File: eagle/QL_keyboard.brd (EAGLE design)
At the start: 66 x 51.4 mm, 40 parts, among them J1 USB-A-S, J2 AVR_SPI_PRG_6TESTPOINTS, U2 3.3V/150mA, U3 MAX3421ESMD, U4 ATMEGA328P_TQFP, U5 TXB0108PW-TSSOP20, Y1 8MHZ

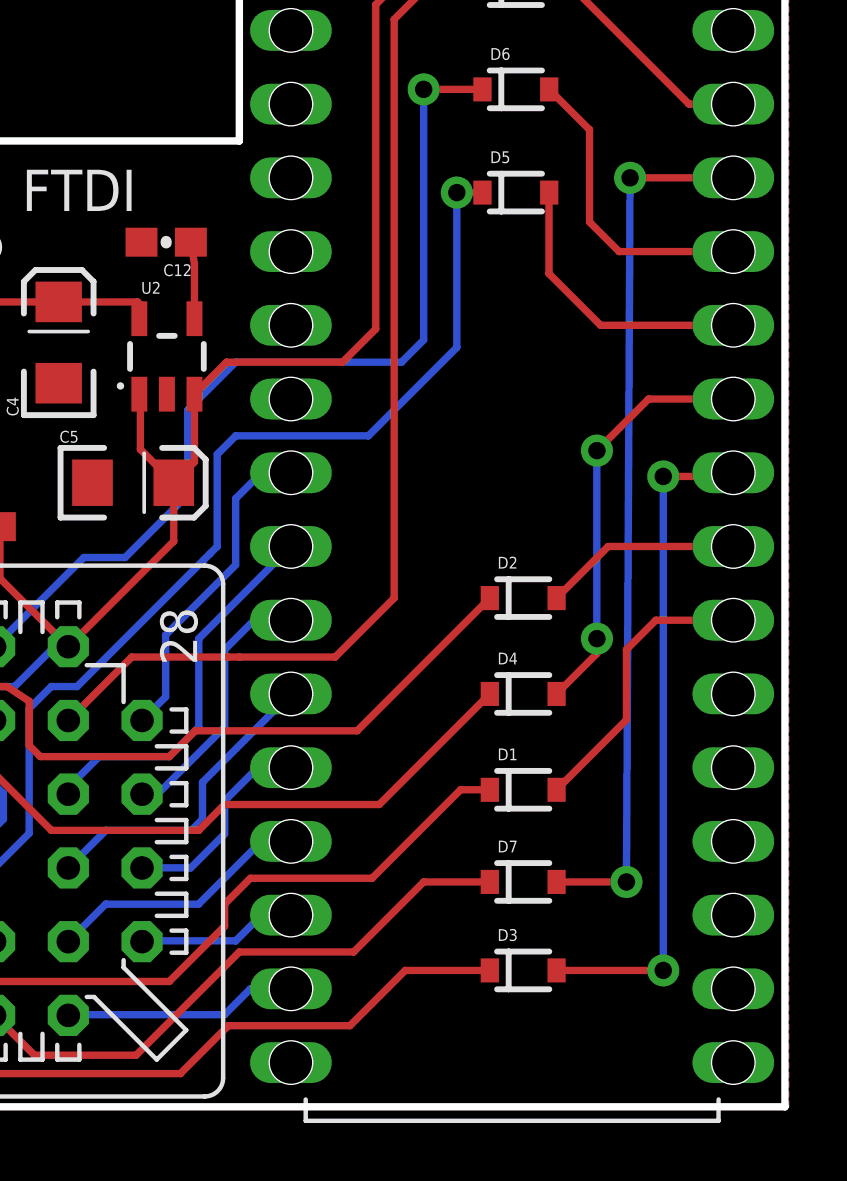
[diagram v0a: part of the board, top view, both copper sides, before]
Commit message: Move diodes out of the way of DIL socket frame
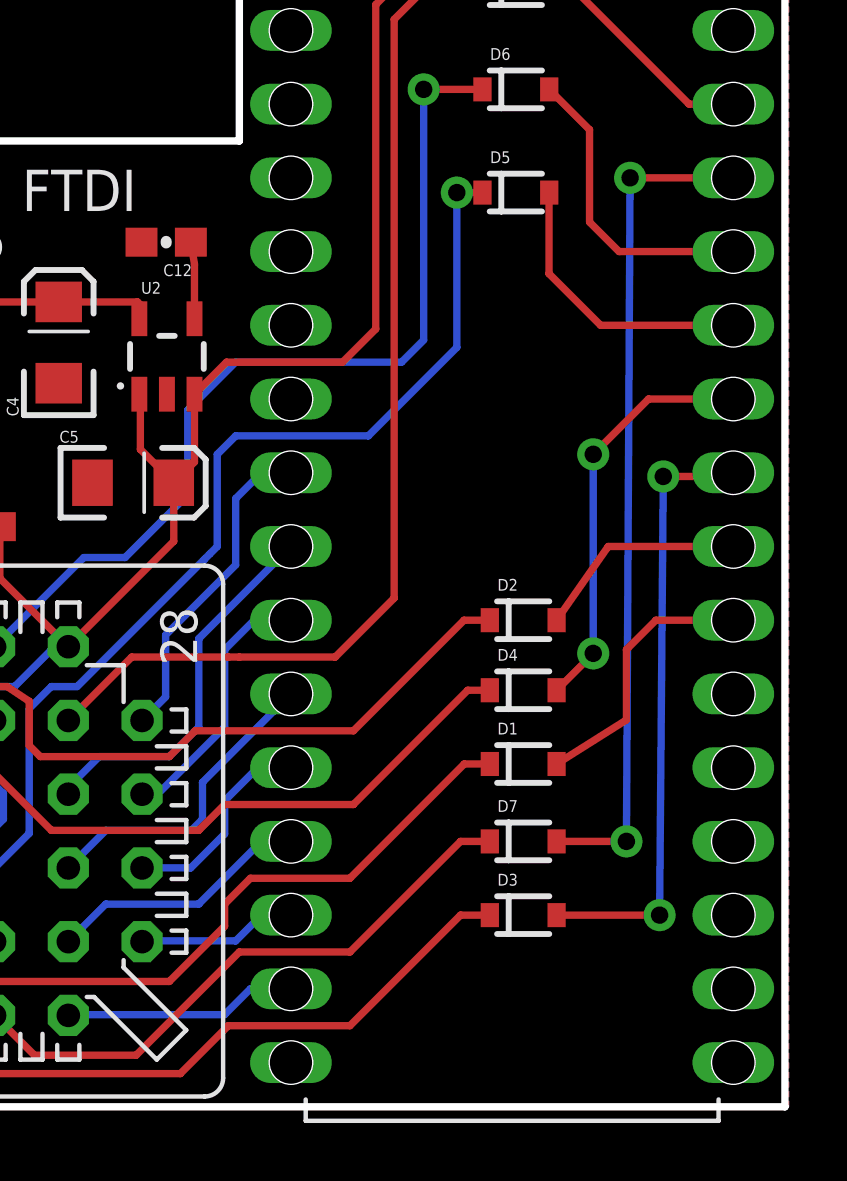
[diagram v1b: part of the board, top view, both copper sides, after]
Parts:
- moved D3 1.91 mm to (70.7, 6.60)
- moved D7 1.40 mm to (70.7, 9.14)
- moved D1 0.89 mm to (70.7, 11.8)
- moved D2 0.76 mm to (70.7, 16.8)
- moved D4 0.13 mm to (70.7, 14.4)
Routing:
- net X2: track 23.5 -> 21.4 mm
- net X6: track 30.2 -> 28.8 mm
- net N$21: track 21.9 -> 22.7 mm
- net X1: track 6.83 -> 7.41 mm
- net N$25: track 20.1 -> 20.7 mm
- net X0: track 9.93 -> 9.37 mm

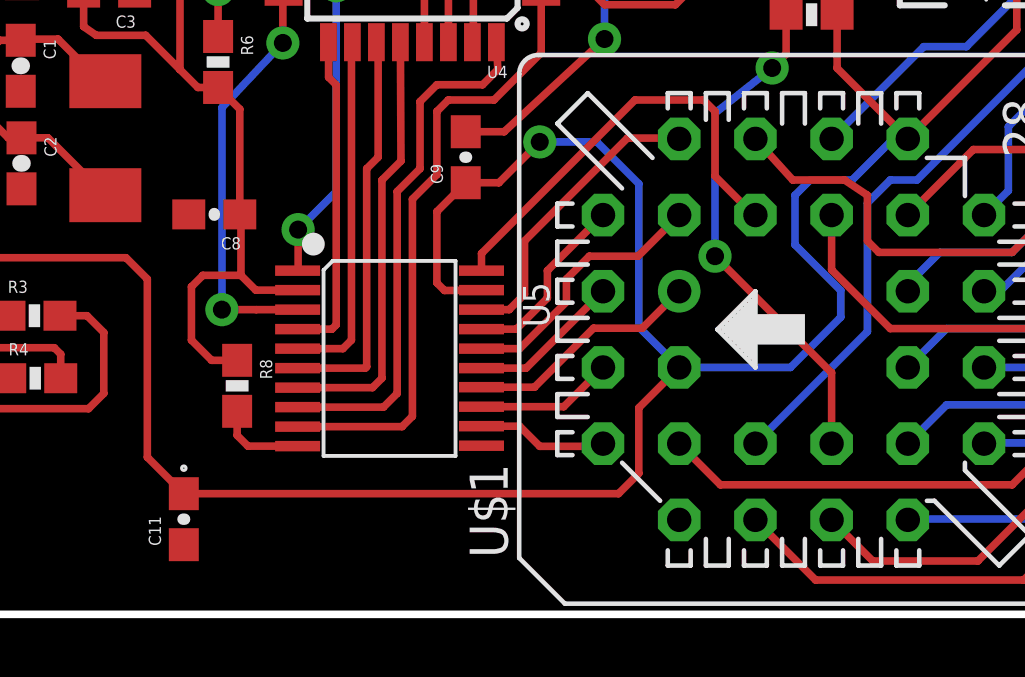
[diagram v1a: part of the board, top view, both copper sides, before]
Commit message: Fix bug in MT8808 VEE connection: connect to GND instead of VCC
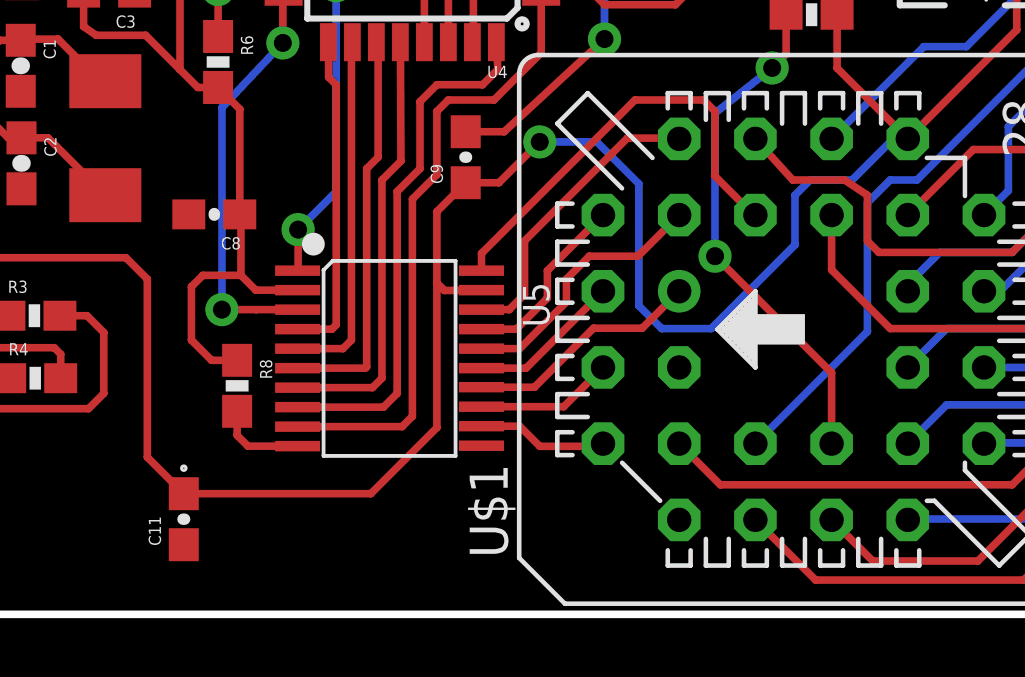
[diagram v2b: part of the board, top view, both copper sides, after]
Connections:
- net GND: now also U$1.3
- net VCC: no longer U$1.3
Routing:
- net VCC: track 128.7 -> 118.3 mm
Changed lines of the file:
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@@
 <layer number="20" name="Dimension" color="15" fill="1" visible="yes" active="yes"/>
 <layer number="21" name="tPlace" color="7" fill="1" visible="yes" active="yes"/>
-<layer number="22" name="bPlace" color="7" fill="1" visible="yes" active="yes"/>
+<layer number="22" name="bPlace" color="7" fill="1" visible="no" active="yes"/>
 <layer number="23" name="tOrigins" color="15" fill="1" visible="yes" active="yes"/>
 <layer number="24" name="bOrigins" color="15" fill="1" visible="yes" active="yes"/>
@@
 <contactref element="R1" pad="2"/>
 <contactref element="U$1" pad="19"/>
-<contactref element="U$1" pad="3"/>
 <contactref element="U2" pad="1"/>
 <contactref element="U2" pad="3"/>
@@
 <wire x1="58.7" y1="21.5" x2="59.4144" y2="22.2144" width="0.254" layer="1"/>
 <wire x1="59.4144" y1="22.2144" x2="59.4144" y2="24.5509" width="0.254" layer="1"/>
-<wire x1="47.4472" y1="8.2296" x2="51.1556" y2="8.2296" width="0.254" layer="16"/>
-<wire x1="51.1556" y1="8.2296" x2="52.832" y2="9.906" width="0.254" layer="16"/>
-<wire x1="52.832" y1="9.906" x2="52.832" y2="10.795" width="0.254" layer="16"/>
-<wire x1="52.832" y1="10.795" x2="51.308" y2="12.319" width="0.254" layer="16"/>
 <wire x1="51.308" y1="12.319" x2="51.308" y2="13.97" width="0.254" layer="16"/>
 <wire x1="51.308" y1="13.97" x2="51.816" y2="14.478" width="0.254" layer="16"/>
@@
 <wire x1="42.799" y1="15.748" x2="44.704" y2="15.748" width="0.254" layer="16"/>
 <wire x1="44.704" y1="15.748" x2="46.101" y2="14.351" width="0.254" layer="16"/>
-<wire x1="46.101" y1="14.351" x2="46.101" y2="9.5758" width="0.254" layer="16"/>
-<wire x1="46.101" y1="9.5758" x2="47.4472" y2="8.2296" width="0.254" layer="16"/>
 <wire x1="40.332" y1="14.387" x2="39.37" y2="13.425" width="0.254" layer="1"/>
 <wire x1="39.37" y1="13.425" x2="39.37" y2="11.049" width="0.254" layer="1"/>
@@
 <wire x1="64.516" y1="25.654" x2="60.5175" y2="25.654" width="0.254" layer="1"/>
 <wire x1="60.5175" y1="25.654" x2="59.4144" y2="24.5509" width="0.254" layer="1"/>
-<wire x1="30.934" y1="4.022" x2="45.424" y2="4.022" width="0.254" layer="1"/>
-<wire x1="45.424" y1="4.022" x2="46.101" y2="4.699" width="0.254" layer="1"/>
-<wire x1="46.101" y1="4.699" x2="46.101" y2="6.8834" width="0.254" layer="1"/>
-<wire x1="46.101" y1="6.8834" x2="47.4472" y2="8.2296" width="0.254" layer="1"/>
 <wire x1="30.607" y1="4.349" x2="30.934" y2="4.022" width="0.254" layer="1"/>
 <wire x1="21.938" y1="11.887" x2="29.007" y2="11.887" width="0.254" layer="1"/>
@@
 <wire x1="29.718" y1="11.176" x2="29.718" y2="5.238" width="0.254" layer="1"/>
 <wire x1="29.718" y1="5.238" x2="30.934" y2="4.022" width="0.254" layer="1"/>
+<wire x1="46.101" y1="14.351" x2="46.101" y2="10.287" width="0.254" layer="16"/>
+<wire x1="46.101" y1="10.287" x2="46.863" y2="9.525" width="0.254" layer="16"/>
+<wire x1="46.863" y1="9.525" x2="48.514" y2="9.525" width="0.254" layer="16"/>
+<wire x1="48.514" y1="9.525" x2="51.308" y2="12.319" width="0.254" layer="16"/>
+<wire x1="39.37" y1="11.049" x2="39.37" y2="6.223" width="0.254" layer="1"/>
+<wire x1="39.37" y1="6.223" x2="37.169" y2="4.022" width="0.254" layer="1"/>
+<wire x1="37.169" y1="4.022" x2="30.934" y2="4.022" width="0.254" layer="1"/>
 </signal>
 <signal name="GND">
@@
 <wire x1="14.732" y1="32.147" x2="16.005" y2="32.147" width="0.254" layer="1"/>
 <wire x1="18.544" y1="23.099" x2="20.139" y2="23.111" width="0.254" layer="1"/>
+<contactref element="U$1" pad="3"/>
 </signal>
 <signal name="3.3V">

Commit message: Minor layout change
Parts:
- moved C7 1.08 mm to (45.8, 22.3)
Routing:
- net GND: track 49.9 -> 53.6 mm
- net 3.3V: track 93.1 -> 93.9 mm
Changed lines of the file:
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@@
 <attribute name="PROD_ID" value="CAP-07888" x="32.077" y="23.365" size="1.778" layer="27" rot="R270" display="off"/>
 </element>
-<element name="C7" library="SparkFun-Capacitors" package="0603-CAP" value="0.1uF" x="46.501" y="23.057" rot="R270">
-<attribute name="PROD_ID" value="CAP-07888" x="46.501" y="23.057" size="1.778" layer="27" rot="R270" display="off"/>
+<element name="C7" library="SparkFun-Capacitors" package="0603-CAP" value="0.1uF" x="45.774" y="22.257" rot="R270">
+<attribute name="PROD_ID" value="CAP-07888" x="45.774" y="22.257" size="1.778" layer="27" rot="R270" display="off"/>
 </element>
 <element name="C8" library="SparkFun-Capacitors" package="0603-CAP" value="0.1uF" x="31.95" y="13.332" rot="R180">
@@
 <wire x1="21.339" y1="23.111" x2="20.139" y2="23.111" width="0.254" layer="1"/>
 <wire x1="40.332" y1="16.087" x2="41.614" y2="16.087" width="0.254" layer="1"/>
-<wire x1="41.614" y1="16.087" x2="44.958" y2="19.177" width="0.254" layer="1"/>
-<via x="44.958" y="19.177" extent="1-16" drill="0.6"/>
-<wire x1="44.958" y1="19.177" x2="44.958" y2="22.098" width="0.254" layer="16"/>
-<via x="44.958" y="22.098" extent="1-16" drill="0.6"/>
-<wire x1="44.958" y1="22.098" x2="46.483" y2="22.225" width="0.254" layer="1"/>
-<wire x1="46.483" y1="22.225" x2="46.501" y2="22.207" width="0.254" layer="1"/>
+<via x="47.531" y="18.877" extent="1-16" drill="0.6"/>
+<wire x1="47.531" y1="18.877" x2="47.531" y2="22.398" width="0.254" layer="16"/>
+<via x="47.531" y="22.398" extent="1-16" drill="0.6"/>
+<wire x1="47.531" y1="22.398" x2="46.756" y2="21.425" width="0.254" layer="1"/>
+<wire x1="46.756" y1="21.425" x2="45.774" y2="21.407" width="0.254" layer="1"/>
 <polygon width="0.254" layer="16" isolate="0.3048">
 <vertex x="13.843" y="0"/>
@@
 <wire x1="18.544" y1="23.099" x2="20.139" y2="23.111" width="0.254" layer="1"/>
 <contactref element="U$1" pad="3"/>
+<wire x1="41.614" y1="16.087" x2="44.404" y2="18.877" width="0.254" layer="1"/>
+<wire x1="44.404" y1="18.877" x2="47.531" y2="18.877" width="0.254" layer="1"/>
 </signal>
 <signal name="3.3V">
@@
 <wire x1="36.084" y1="24.565" x2="35.284" y2="25.365" width="0.254" layer="1"/>
 <wire x1="35.284" y1="25.365" x2="34.2614" y2="25.365" width="0.254" layer="1"/>
-<wire x1="45.231" y1="23.946" x2="46.501" y2="23.907" width="0.254" layer="1"/>
-<wire x1="46.501" y1="23.907" x2="47.478" y2="23.907" width="0.254" layer="1"/>
-<wire x1="47.478" y1="23.907" x2="48.787" y2="25.47" width="0.254" layer="1"/>
-<wire x1="48.787" y1="25.47" x2="49.041" y2="25.724" width="0.254" layer="1"/>
 <wire x1="49.041" y1="25.724" x2="49.041" y2="28.645" width="0.254" layer="1"/>
 <wire x1="49.041" y1="28.645" x2="51.327" y2="28.645" width="0.254" layer="1"/>
@@
 <wire x1="31.188" y1="10.919" x2="31.569" y2="11.3" width="0.254" layer="1"/>
 <wire x1="31.569" y1="11.3" x2="32.839" y2="11.3" width="0.254" layer="1"/>
-<wire x1="42.8466" y1="24.565" x2="44.612" y2="24.565" width="0.254" layer="1"/>
-<wire x1="44.612" y1="24.565" x2="45.231" y2="23.946" width="0.254" layer="1"/>
-<wire x1="42.8466" y1="22.965" x2="44.25" y2="22.965" width="0.254" layer="1"/>
-<wire x1="44.25" y1="22.965" x2="45.231" y2="23.946" width="0.254" layer="1"/>
 <wire x1="46.247" y1="31.623" x2="46.247" y2="31.439" width="0.254" layer="1"/>
 <wire x1="46.247" y1="31.439" x2="49.041" y2="28.645" width="0.254" layer="1"/>
@@
 <wire x1="20.828" y1="22.098" x2="20.972" y2="22.098" width="0.254" layer="1"/>
 <wire x1="20.972" y1="22.098" x2="21.971" y2="21.099" width="0.254" layer="1"/>
+<wire x1="42.8466" y1="24.565" x2="44.142" y2="24.565" width="0.254" layer="1"/>
+<wire x1="44.142" y1="24.565" x2="45.6" y2="23.107" width="0.254" layer="1"/>
+<wire x1="45.6" y1="23.107" x2="45.774" y2="23.107" width="0.254" layer="1"/>
+<wire x1="42.8466" y1="22.965" x2="45.632" y2="22.965" width="0.254" layer="1"/>
+<wire x1="45.632" y1="22.965" x2="45.774" y2="23.107" width="0.254" layer="1"/>
+<wire x1="49.041" y1="25.724" x2="46.424" y2="23.107" width="0.254" layer="1"/>
+<wire x1="46.424" y1="23.107" x2="45.774" y2="23.107" width="0.254" layer="1"/>
 </signal>
 <signal name="SS">

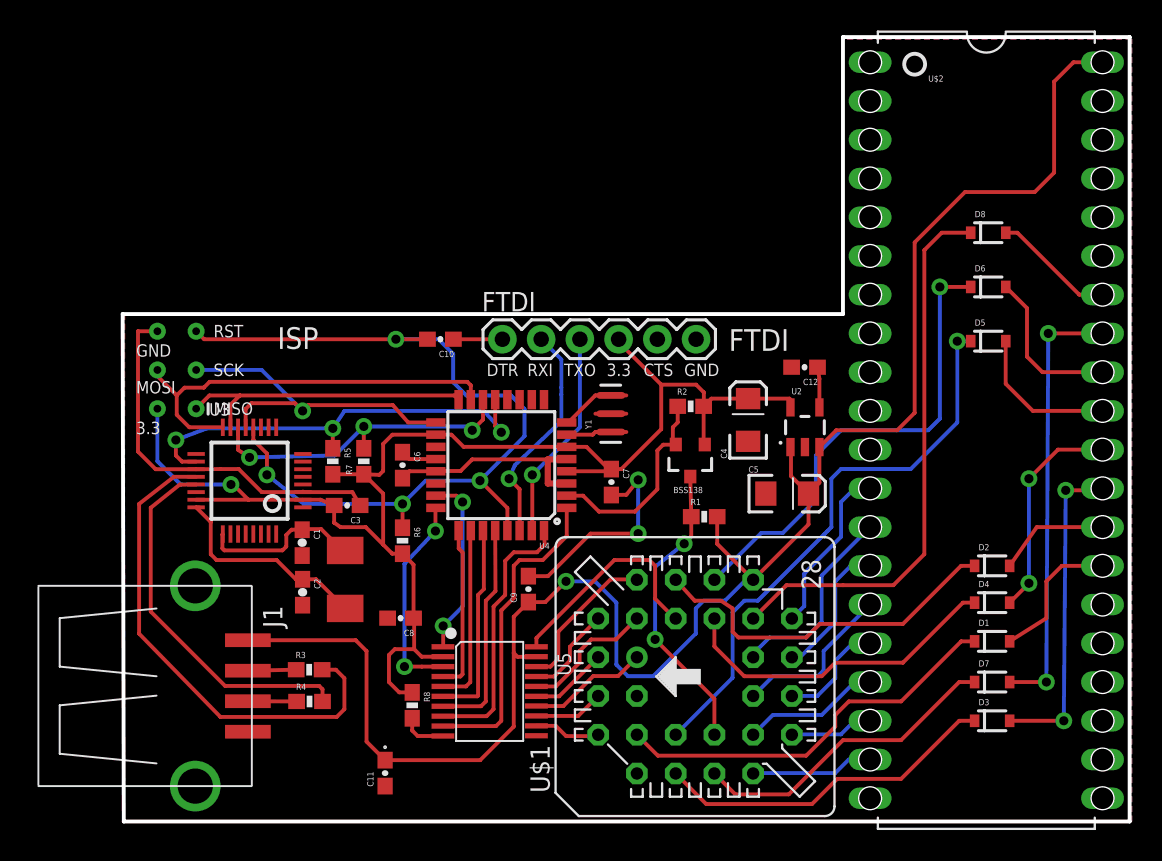
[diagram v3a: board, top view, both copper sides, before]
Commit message: Change MT8808 package to SMD PLCC28 holder.
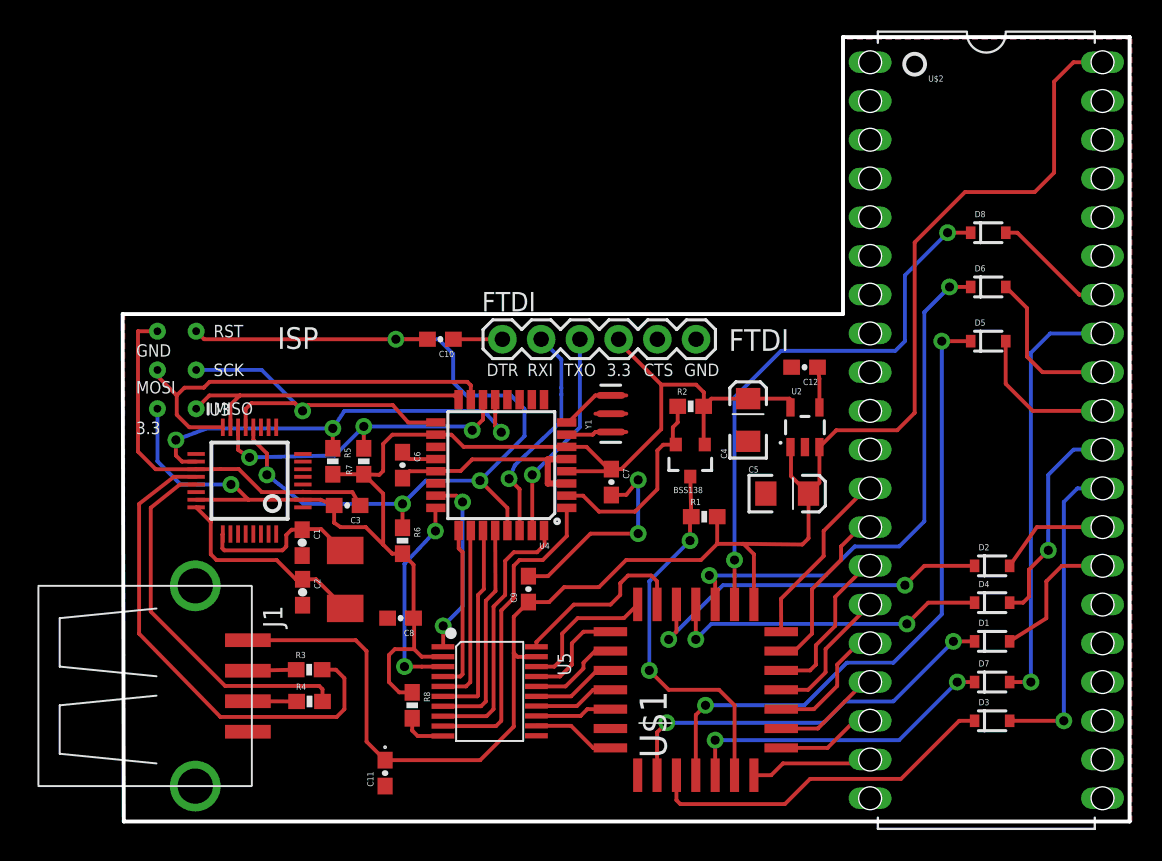
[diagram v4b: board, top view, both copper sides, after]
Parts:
- U$1: value MT8808 -> MT8808SMD; device ppe_custom:S28 -> ppe_custom:PLCC28S
- moved U$1 0.87 mm to (51.3, 8.64)
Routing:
- net VCC: track 118.3 -> 111.3 mm, vias 1 -> 0
- net RST8808V5: track 19.7 -> 25.0 mm
- net N$23: track 37.5 -> 42.6 mm, vias 1 -> 2
- net N$24: track 31.5 -> 35.1 mm, vias 1 -> 2
- net AY0: track 8.88 -> 6.03 mm
- net AY2: track 7.91 -> 5.29 mm
- net AX0: track 14.7 -> 12.1 mm
- net Y5: track 9.10 -> 7.09 mm
- net Y3: track 10.9 -> 9.04 mm
- net Y1: track 13.1 -> 11.4 mm
- net Y2: track 9.18 -> 10.5 mm
- net Y4: track 7.23 -> 8.44 mm
- net N$13: track 4.37 -> 5.45 mm
- net Y6: track 5.51 -> 6.57 mm
- net N$21: track 22.7 -> 23.6 mm
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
